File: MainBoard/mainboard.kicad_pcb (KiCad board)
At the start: 2 copper layers, 32 x 32 mm, 46 parts, among them J1 MatrixOut, J3 prog, J4 MatrixPin, J5 PowerIn, Q2 AO3401A, U1 W25Q128JVS, U2 RP2040, U3 LIS3DH, U4 AT42QT1011-TSHR, Y1 12MHz

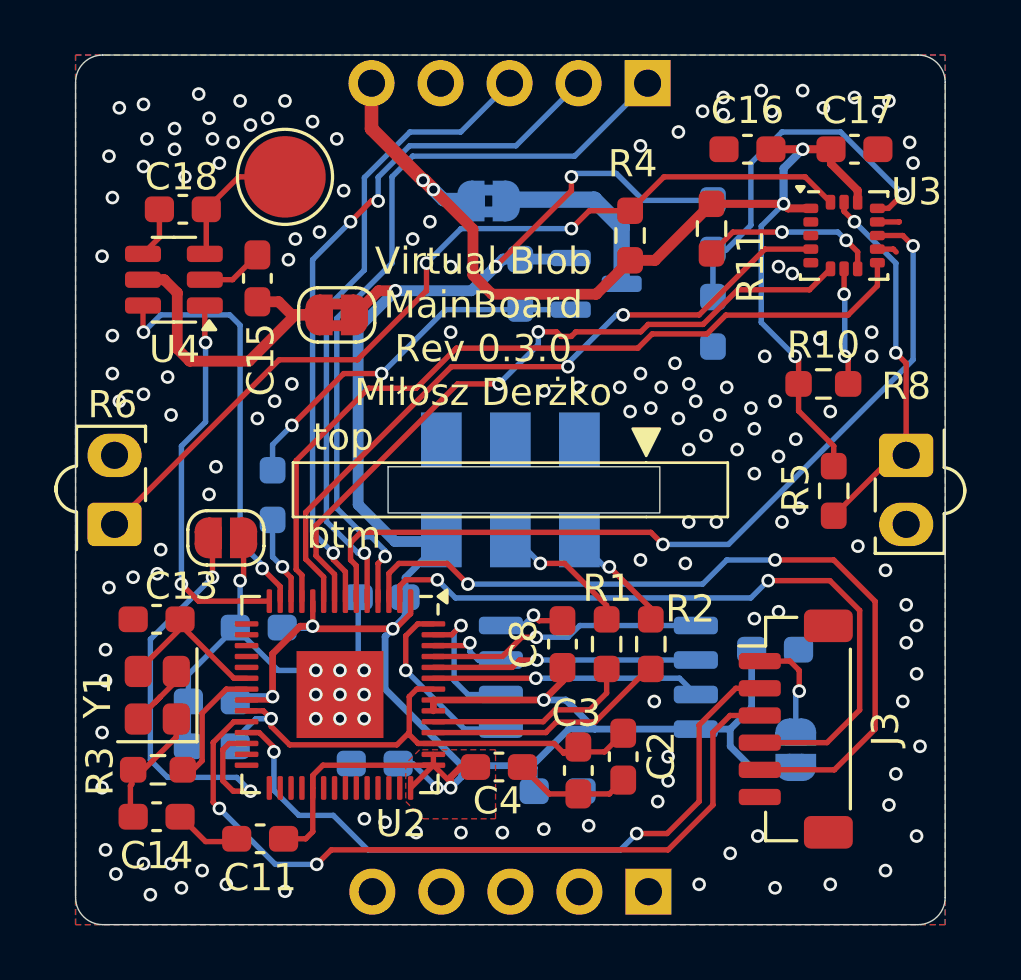
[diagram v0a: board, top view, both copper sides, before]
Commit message: Change location of tuch sensor, touch button now power up all components, change length. Add buzzer to mainboard and remove touch from them. change revision version
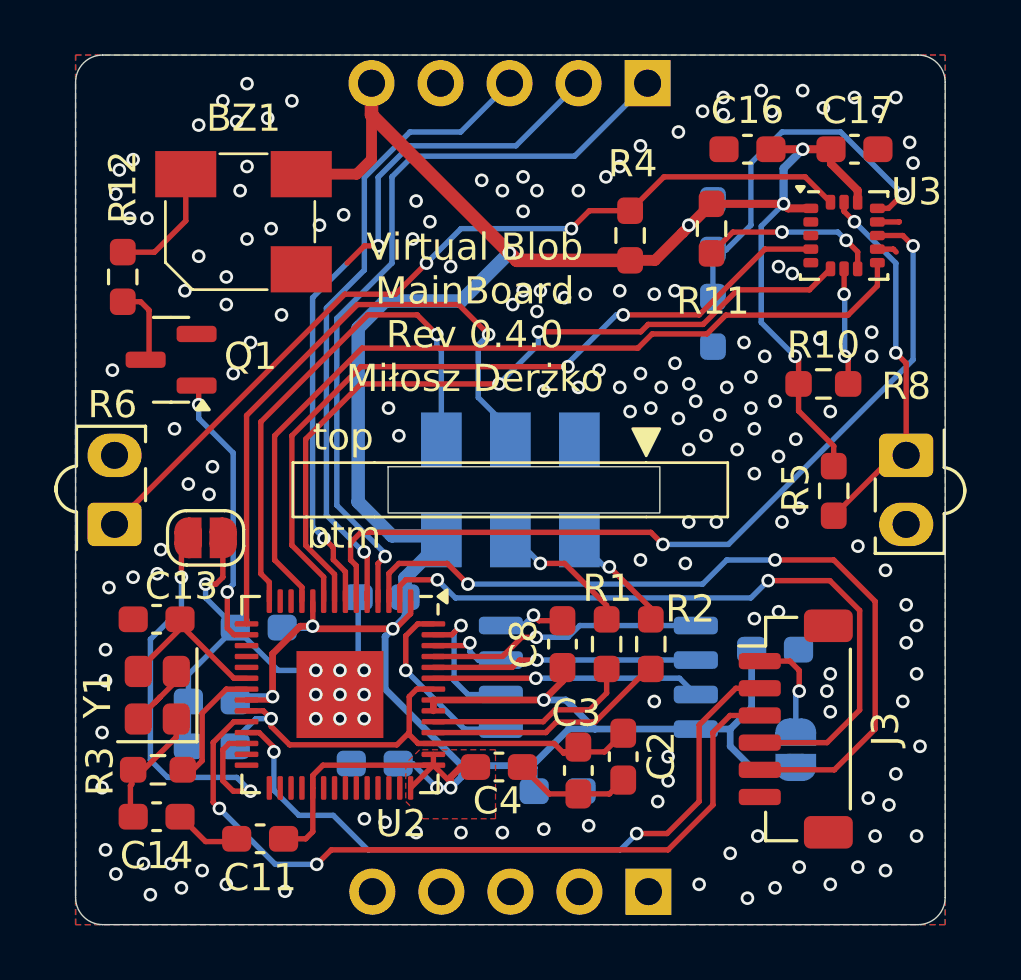
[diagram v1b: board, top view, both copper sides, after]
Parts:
- removed C15: 100n, Capacitor_SMD:C_0603_1608Metric_Pad1.08x0.95mm_HandSolder
- removed C18: 2n, Capacitor_SMD:C_0603_1608Metric_Pad1.08x0.95mm_HandSolder
- removed JP4: touch_pwr, Jumper:SolderJumper-2_P1.3mm_Bridged2Bar_RoundedPad1.0x1.5mm
- removed JP5: sens_pwr, Jumper:SolderJumper-2_P1.3mm_Bridged2Bar_RoundedPad1.0x1.5mm
- removed Q2: AO3401A, Package_TO_SOT_SMD:SOT-23
- removed R13: 100, Resistor_SMD:R_0603_1608Metric_Pad0.98x0.95mm_HandSolder
- removed TP4: TOUCH, TestPoint:TestPoint_Pad_D3.0mm
- removed U4: AT42QT1011-TSHR, Package_TO_SOT_SMD:SOT-23-6
- added BZ1: Buzzer, Buzzer_Beeper:Buzzer_Murata_PKMCS0909E, F.Cu at (186.1, 56.1)
- added Q1: AO3400A, Package_TO_SOT_SMD:SOT-23, F.Cu at (183.5, 61.2)
- R12: value 100k -> 100; moved to F.Cu
- moved R12 14.6 mm to (181.7, 58.2)
- moved JP2 0.75 mm to (184.8, 67.8)
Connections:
- C16 pad 2: VBUS -> VCC
- C17 pad 2: VBUS -> VCC
- J1 pad 5: VBUS -> VCC
- J5 pad 4: unconnected-(J5-Pin_4-Pad4) -> /CPU/TOUCH
- J5 pad 5: unconnected-(J5-Pin_5-Pad5) -> /CPU/PWR_LATCH
- R10 pad 1: VBUS -> VCC
- R11 pad 1: VBUS -> VCC
- R12 pad 1: VCC -> Net-(BZ1--)
- R4 pad 1: VBUS -> VCC
- R5 pad 1: VBUS -> VCC
- U2 pad 12: /CPU/SENS_PWR -> unconnected-(U2-GPIO9-Pad12)
- U2 pad 13: /CPU/TOUCH_SYNC -> unconnected-(U2-GPIO10-Pad13)
- U2 pad 15: unconnected-(U2-GPIO12-Pad15) -> /CPU/PWR_LATCH
- U2 pad 16: unconnected-(U2-GPIO13-Pad16) -> /CPU/BUZZ
- U3 pad 1: VBUS -> VCC
- U3 pad 14: VBUS -> VCC
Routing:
- net VBUS: track 42.3 -> 0.00 mm, vias 5 -> 0
- net VCC: track 95.2 -> 127.1 mm, vias 9 -> 11
- net /CPU/PWR_LATCH: track 0.00 -> 23.2 mm, vias 0 -> 1
- net /CPU/TOUCH_SYNC: track 15.7 -> 0.00 mm, vias 2 -> 0
- net Net-(JP4-A): track 12.1 -> 0.00 mm
- net Net-(Q1-D): track 14.0 -> 2.97 mm, vias 2 -> 0
- net /CPU/BUZZ: track 0.00 -> 10.4 mm, vias 0 -> 2
- net Net-(JP5-A): track 6.78 -> 0.00 mm
- net Net-(U4-SNSK): track 5.05 -> 0.00 mm
- net /CPU/TOUCH: track 14.1 -> 19.1 mm, vias 2 -> 1
- net Net-(BZ1--): track 0.00 -> 4.51 mm
- net /CPU/SENS_PWR: track 3.27 -> 0.00 mm, vias 1 -> 0
- net /CPU/I2C_SCL: track 26.2 -> 28.6 mm
- net /CPU/I2C_SDA: track 26.3 -> 28.6 mm
- net Net-(U4-SNS): track 1.89 -> 0.00 mm
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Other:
- board text added: "Virtual Blob MainBoard Rev 0.4.0 Miłosz Derżko"
- board text removed: "Virtual Blob MainBoard Rev 0.3.0 Miłosz Derżko"

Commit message: add buzer, update layout to schematic, make pcb mounting
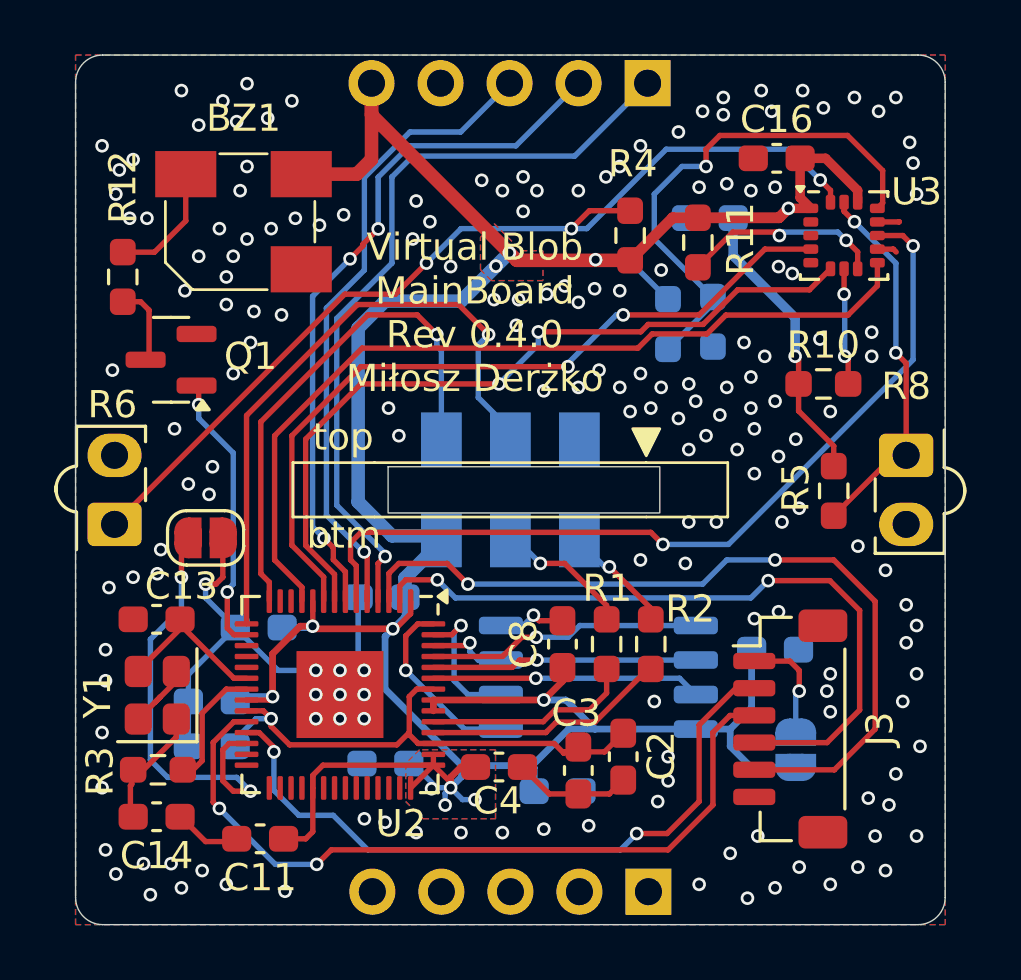
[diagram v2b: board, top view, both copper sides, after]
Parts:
- BZ1: footprint Buzzer_Beeper:Buzzer_Murata_PKMCS0909E -> buzzer:Buzzer_SMD_5020
- C17: moved to B.Cu
- moved C17 5.90 mm to (203.3, 56.0), turned to 0 degrees
- moved R7 4.00 mm to (201.8, 59.9)
- moved C16 1.13 mm to (205.8, 53.8)
- moved R11 0.72 mm to (202.9, 56.9)
- moved C5 0.39 mm to (191.4, 76.1)
- moved J3 0.20 mm to (206.3, 74.8)
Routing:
- net /utils/BAT_LVL: track 14.0 -> 19.0 mm
- net /utils/OPTO1: track 32.0 -> 35.6 mm, vias 2 -> 3
- net VCC: track 127.1 -> 129.9 mm, vias 11 -> 13
- net /utils/CS: track 6.63 -> 7.45 mm
- net /CS: track 26.2 -> 25.9 mm, vias 2 -> 3
- net GND: vias 166 -> 180
- net (no net): vias 4 -> 0
- added copper zone on B.Cu, net VCC

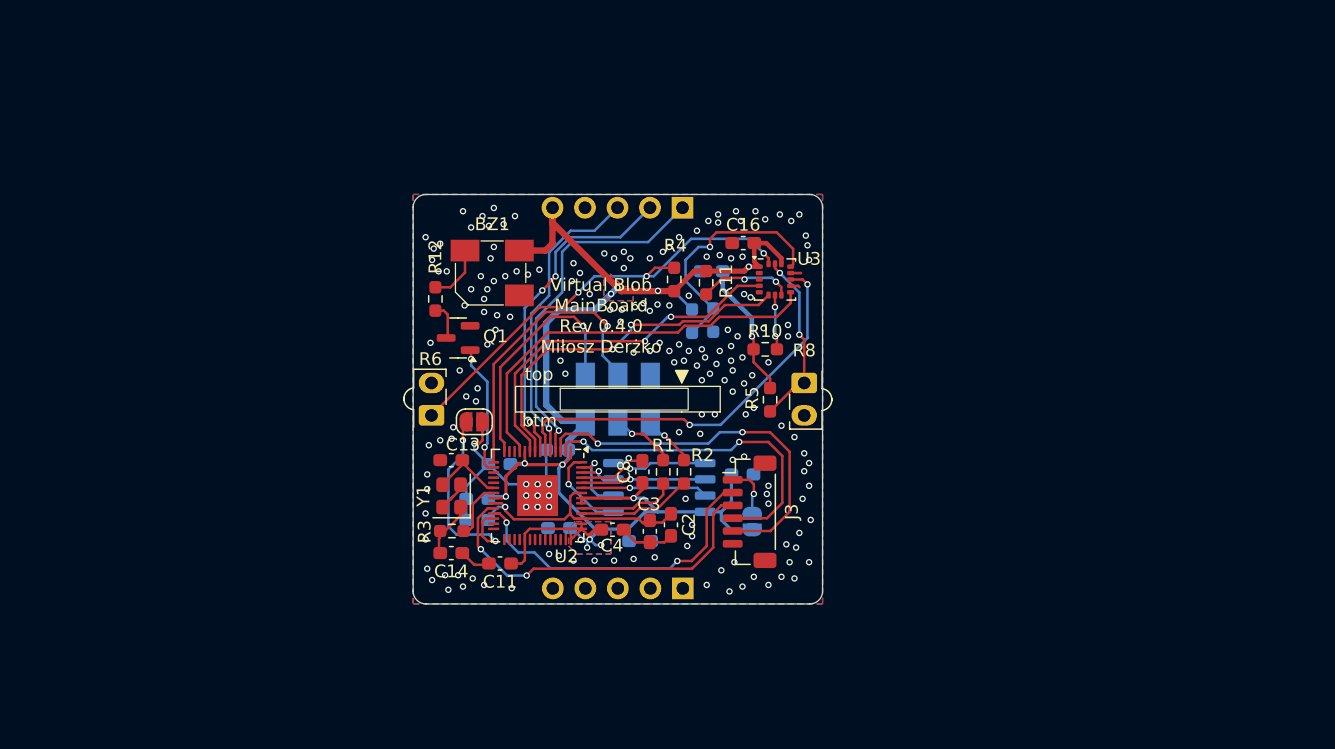
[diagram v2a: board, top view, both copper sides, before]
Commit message: some changes for esp32 board
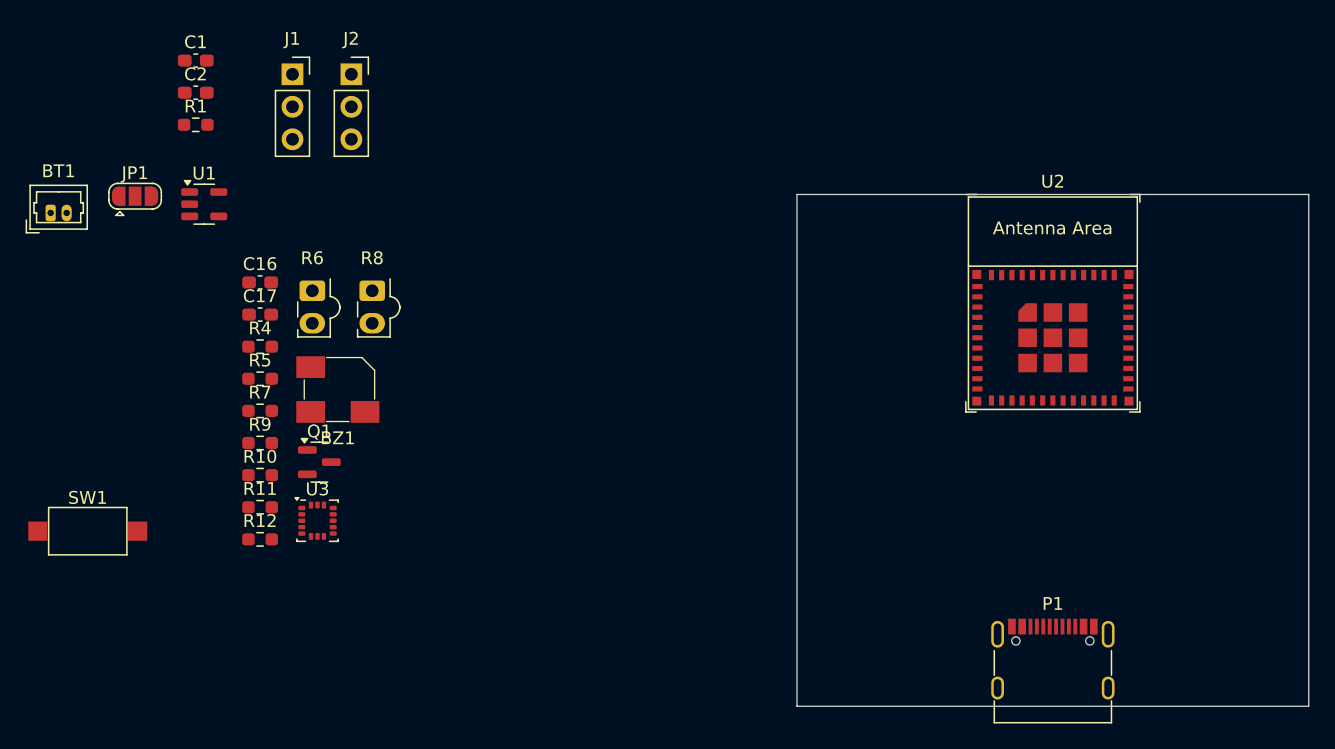
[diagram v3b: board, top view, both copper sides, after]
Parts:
- removed C10, C11, C12, C5, C6, C7, C8, C9: 100n, Capacitor_SMD:C_0603_1608Metric_Pad1.08x0.95mm_HandSolder
- removed C13, C14: 15p, Capacitor_SMD:C_0603_1608Metric_Pad1.08x0.95mm_HandSolder
- removed C3, C4: 1u, Capacitor_SMD:C_0603_1608Metric_Pad1.08x0.95mm_HandSolder
- removed J3: prog, Connector_JST:JST_SH_BM06B-SRSS-TB_1x06-1MP_P1.00mm_Vertical
- removed J4: MatrixPin, Connector_PinSocket_2.54mm:PinSocket_1x05_P2.54mm_Vertical
- removed J5: PowerIn, EdgeConn:edge_conn_03x02_1_6x10mm_socket
- removed JP2: RST, Jumper:SolderJumper-2_P1.3mm_Open_RoundedPad1.0x1.5mm
- removed JP3: prog_pwr, Jumper:SolderJumper-2_P1.3mm_Open_RoundedPad1.0x1.5mm
- removed R2: 27R, Resistor_SMD:R_0603_1608Metric_Pad0.98x0.95mm_HandSolder
- removed R3: 1k, Resistor_SMD:R_0603_1608Metric_Pad0.98x0.95mm_HandSolder
- removed Y1: 12MHz, Crystal:Crystal_SMD_2520-4Pin_2.5x2.0mm
- added BT1: Battery_Cell, Connector_Molex:Molex_PicoBlade_53047-0210_1x02_P1.25mm_Vertical, F.Cu at (151.7, 51.4)
- added J2: Matrix_in, Connector_PinSocket_2.54mm:PinSocket_1x03_P2.54mm_Vertical, F.Cu at (175.2, 40.6)
- added JP1: PROG_PIN, Jumper:SolderJumper-3_P1.3mm_Open_RoundedPad1.0x1.5mm, F.Cu at (158.3, 50.1)
- added P1: USB_C_Receptacle_USB2.0_14P, Connector_USB:USB_C_Receptacle_G-Switch_GT-USB-7010ASV, F.Cu at (230.0, 87.5)
- added SW1: SW_Push, Button_Switch_SMD:SW_SPST_CK_RS282G05A3, F.Cu at (154.6, 76.3)
- C1: value 100n -> 1u; moved to F.Cu
- C17, R7, R9: moved to F.Cu
- C2: value 100n -> 1u
- J1: value MatrixOut -> Matrix_power; footprint Connector_PinSocket_2.54mm:PinSocket_1x05_P2.54mm_Vertical -> Connector_PinSocket_2.54mm:PinSocket_1x03_P2.54mm_Vertical; moved to F.Cu
- R1: value 27R -> 5.1k
- U1: value W25Q128JVS -> MCP73811T-420I-OT; footprint Package_SO:SOIC-8_5.3x5.3mm_P1.27mm -> Package_TO_SOT_SMD:SOT-23-5; moved to F.Cu
- U2: value RP2040 -> ESP32-C3-MINI-1; footprint Package_DFN_QFN:QFN-56-1EP_7x7mm_P0.4mm_EP3.2x3.2mm -> PCM_Espressif:ESP32-C3-MINI-1
- moved C2 50.2 mm to (163.0, 42.0), turned to 0 degrees
- moved R1 45.5 mm to (163.0, 44.6), turned to 0 degrees
- moved U2 43.0 mm to (230.0, 58.5), turned to 0 degrees
- moved C1 42.1 mm to (163.0, 39.5), turned to 0 degrees
- moved U1 41.9 mm to (163.7, 50.8)
- moved R10 40.7 mm to (168.0, 71.9)
- moved U3 40.4 mm to (172.5, 75.5)
- moved R5 39.9 mm to (168.0, 64.4), turned to 0 degrees
- moved R11 39.0 mm to (168.0, 74.4), turned to 0 degrees
- moved C16 37.9 mm to (168.0, 56.9)
- moved R9 36.7 mm to (168.0, 69.4), turned to 0 degrees
- moved C17 35.5 mm to (168.0, 59.4)
- moved R8 34.5 mm to (176.8, 57.5)
- moved R7 34.5 mm to (168.0, 66.9), turned to 0 degrees
- moved R4 32.8 mm to (168.0, 61.9), turned to 0 degrees
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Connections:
- C1 pad 1: +1V1 -> VCC
- C2 pad 1: +1V1 -> +5V
- J1 pad 1: /SCK -> VCC
- J1 pad 2: /CS -> GND
- J1 pad 3: /MOSI -> unconnected-(J1-Pin_3-Pad3)
- R1 pad 1: /CPU/USB_RP+ -> Net-(P1-CC1)
- R1 pad 2: /CPU/USB+ -> GND
- U1 pad 1: /CPU/QSPI_SS -> +5V
- U1 pad 2: /CPU/QSPI_SD1 -> GND
- U1 pad 3: /CPU/QSPI_SD2 -> VCC
- U1 pad 4: GND -> +5V
- U1 pad 5: /CPU/QSPI_SD0 -> Net-(JP1-C)
- U2 pad 1: VCC -> GND
- U2 pad 10: VCC -> unconnected-(U2-NC-Pad10)
- U2 pad 11: /CPU/ACCEL_INT2 -> GND
- U2 pad 14: /CPU/TOUCH -> GND
- U2 pad 15: /CPU/PWR_LATCH -> unconnected-(U2-NC-Pad15)
- U2 pad 18: unconnected-(U2-GPIO15-Pad18) -> /CPU/TOUCH
- U2 pad 19: unconnected-(U2-TESTEN-Pad19) -> /DATA_MATRIX
- U2 pad 2: /CPU/UART_TX -> GND
- U2 pad 20: /CPU/XIN -> /CPU/I2C_SDA
- U2 pad 21: /CPU/XOUT -> /CPU/I2C_SCL
- U2 pad 22: VCC -> /CPU/ACCEL_INT2
- U2 pad 23: +1V1 -> /CPU/ACCEL_INT1
- U2 pad 24: /CPU/SWCLK -> unconnected-(U2-NC-Pad24)
- U2 pad 25: /CPU/SWDIO -> unconnected-(U2-NC-Pad25)
- U2 pad 26: Net-(JP2-B) -> /CPU/USB-
- U2 pad 27: unconnected-(U2-GPIO16-Pad27) -> /CPU/USB+
- U2 pad 3: /CPU/UART_RX -> VCC
- U2 pad 33: VCC -> unconnected-(U2-NC-Pad33)
- U2 pad 36: unconnected-(U2-GPIO24-Pad36) -> GND
- U2 pad 37: unconnected-(U2-GPIO25-Pad37) -> GND
- U2 pad 38: unconnected-(U2-GPIO26_ADC0-Pad38) -> GND
- U2 pad 39: unconnected-(U2-GPIO27_ADC1-Pad39) -> GND
- U2 pad 4: /SCK -> unconnected-(U2-NC-Pad4)
- U2 pad 40: unconnected-(U2-GPIO28_ADC2-Pad40) -> GND
- U2 pad 41: unconnected-(U2-GPIO29_ADC3-Pad41) -> GND
- U2 pad 42: VCC -> GND
- U2 pad 43: VCC -> GND
- U2 pad 44: VCC -> GND
- U2 pad 45: +1V1 -> GND
- U2 pad 46: /CPU/USB_RP- -> GND
- U2 pad 47: /CPU/USB_RP+ -> GND
- U2 pad 48: VCC -> GND
- U2 pad 49: VCC -> GND
- U2 pad 5: /MOSI -> unconnected-(U2-GPIO2/ADC1_CH2-Pad5)
- U2 pad 50: +1V1 -> GND
- U2 pad 51: /CPU/QSPI_SD3 -> GND
- U2 pad 52: /CPU/QSPI_SCLK -> GND
- U2 pad 53: /CPU/QSPI_SD0 -> GND
- U2 pad 6: /CPU/ACCEL_INT1 -> unconnected-(U2-GPIO3/ADC1_CH3-Pad6)
- U2 pad 7: /CS -> unconnected-(U2-NC-Pad7)
- U2 pad 8: /CPU/I2C_SDA -> /CPU/EN
- U2 pad 9: /CPU/I2C_SCL -> unconnected-(U2-NC-Pad9)
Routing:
- net VCC: track 129.9 -> 0.00 mm, vias 13 -> 0
- net /utils/OPTO1: track 35.6 -> 0.00 mm, vias 3 -> 0
- net /CPU/ACCEL_INT2: track 31.8 -> 0.00 mm
- net /CPU/ACCEL_INT1: track 31.8 -> 0.00 mm, vias 2 -> 0
- net /CPU/UART_RX: track 30.2 -> 0.00 mm, vias 2 -> 0
- net GND: track 30.0 -> 0.00 mm, vias 180 -> 0
- net /CPU/I2C_SCL: track 28.6 -> 0.00 mm, vias 2 -> 0
- net /CPU/I2C_SDA: track 28.6 -> 0.00 mm, vias 2 -> 0
- net /CPU/SWCLK: track 28.4 -> 0.00 mm, vias 2 -> 0
- net /SCK: track 28.1 -> 0.00 mm, vias 1 -> 0
- net /CPU/UART_TX: track 26.6 -> 0.00 mm, vias 2 -> 0
- net /CS: track 25.9 -> 0.00 mm, vias 3 -> 0
- net /CPU/SWDIO: track 25.5 -> 0.00 mm, vias 2 -> 0
- net /MOSI: track 23.6 -> 0.00 mm, vias 1 -> 0
- net /CPU/PWR_LATCH: track 23.2 -> 0.00 mm, vias 1 -> 0
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- removed copper zone on B.Cu, net GND
- removed copper zone on F.Cu, net GND
- removed copper zone on B.Cu, net VCC
- removed copper zone on F.Cu, net VCC
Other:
- board size 32 x 32 mm -> 40 x 40 mm
- board text removed: "Virtual Blob MainBoard Rev 0.4.0 Miłosz Derżko"

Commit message: change schematic
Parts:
- moved BZ1 10.4 mm to (182.5, 59.0)
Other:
- board size 40 x 40 mm -> 32 x 40 mm
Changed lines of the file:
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@@
 	(footprint "buzzer:Buzzer_SMD_5020"
 		(layer "F.Cu")
-		(at 174.24 65.245)
+		(at 182.5 59)
 		(descr "Murata Buzzer http://www.murata.com/en-us/api/pdfdownloadapi?cate=&partno=PKMCS0909E4000-R1")
 		(tags "Murata Buzzer Beeper")
@@
 	)
 	(gr_rect
-		(start 210 50)
-		(end 250 90)
+		(start 214 50)
+		(end 246 90)
 		(stroke
 			(width 0.05)
